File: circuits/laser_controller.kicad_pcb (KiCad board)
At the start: 4 copper layers, 173 x 61.1 mm, 180 parts, among them J1 USB_MINI_B, J2 USB_MINI_B, J5 24V DC IN, J6 CONN_RJ45, Q1 SOT-23, Q2 SOT-23, Q3 SOT-23, Q4 SOT-23, Q5 SOT-23, Q6 SOT-23, SW1 SW_PUSH, SW2 SW_PUSH, SW3 SW_PUSH, U1 SOIC-8_3.9x4.9mm_P1.27mm, U10 QFN-28-1EP_5x5mm_P0.5mm_EP3.3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, U11 SOT-23-5, U12 TSSOP-14_4.4x5mm_P0.65mm, U13 SOT-23, U14 LQFP-64_10x10mm_P0.5mm, U15 TSOT-23-6, U16 TSOT-23-6, U2 SOIC-8_3.9x4.9mm_P1.27mm, U3 SOIC-8_3.9x4.9mm_P1.27mm, U4 SOIC-8_3.9x4.9mm_P1.27mm, U5 SOT-23-5, U6 SOT-23-5, U7 SOT-23-5, U8 SOT-23-5, U9 ESP32-S3-WROOM-1

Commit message: fix(pcb): pull D8/C42 back from the board edge
D8 and C42 landed with negative edge clearance (-0.708mm / -0.055mm)
after the courtyard-overlap fix -- close enough to J1's cluster that
the solver satisfied the no-overlap constraint by pushing them partly
off the board outline instead. Re-solved both with an explicit board-
edge margin this time; still zero courtyard/pad overlaps.

Caught this because routing generated against the previous positions
produced segments with endpoints outside the board outline near D8 --
a good reminder to check edge clearance, not just inter-component
clearance, whenever placement changes.
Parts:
- moved D8 8.60 mm to (32.3, 81.3)
- moved C42 6.50 mm to (50.4, 83.9)
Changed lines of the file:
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@@
   )
   (footprint "D_SOD-523" (layer "F.Cu")
-    (at 40.893 80.417 90)
+    (at 32.340 81.316 90)
     (descr "http://www.diodes.com/datasheets/ap02001.pdf p.144")
     (tags "Diode SOD523")
@@
   )
   (footprint "C_0805_2012Metric_Pad1.18x1.45mm_HandSolder" (layer "F.Cu")
-    (at 44.675 80.800)
+    (at 50.402 83.875)
     (descr "Capacitor SMD 0805 (2012 Metric), square (rectangular) end terminal, IPC_7351 nominal with elongated pad for handsoldering. (Body size source: IPC-SM-782 page 76, https://www.pcb-3d.com/wordpress/wp-content/uploads/ipc-sm-782a_amendment_1_and_2.pdf, https://docs.google.com/spreadsheets/d/1BsfQQcO9C6DZCsRaXUlFlo91Tg2WpOkGARC1WS5S8t0/edit?usp=sharing), generated with kicad-footprint-generator")
     (tags "capacitor handsolder")

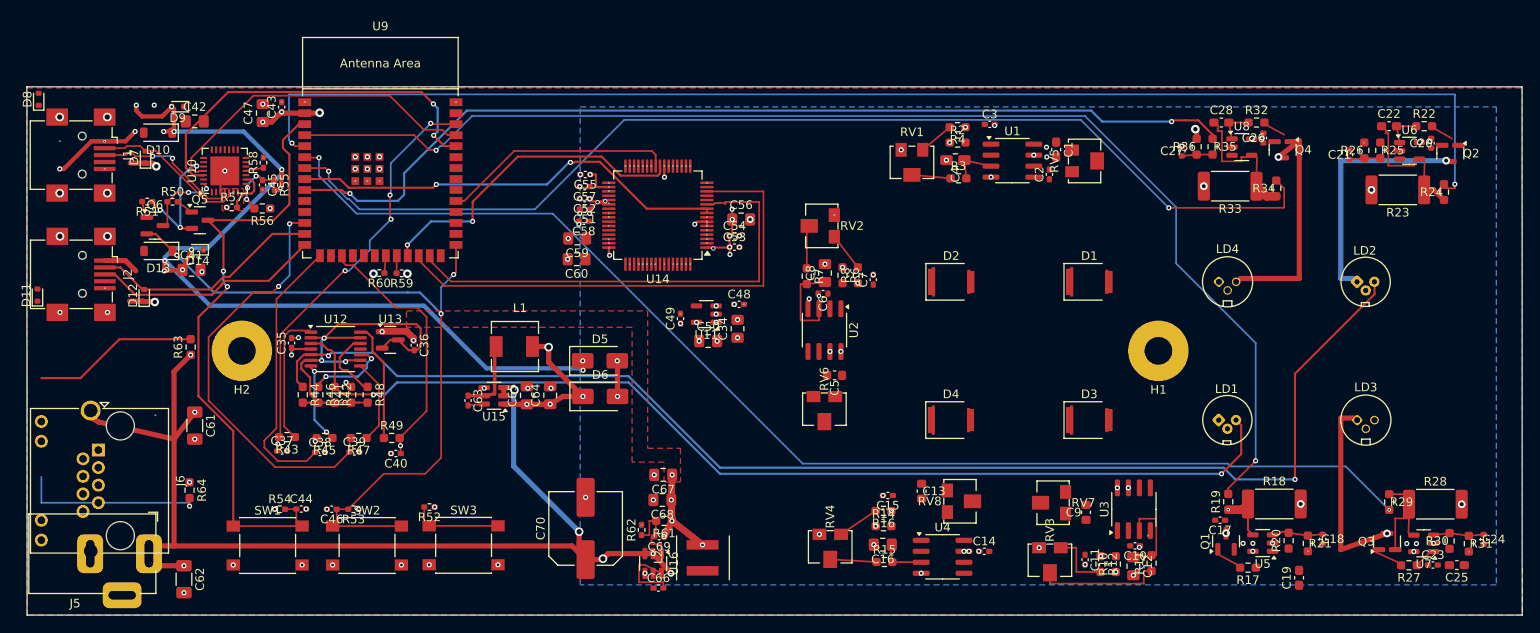
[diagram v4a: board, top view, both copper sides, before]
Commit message: fix(pcb): regenerate routing with clean power planes and full connectivity closure
Full re-route of laser_controller.kicad_pcb using the fixed router
engine (no via-on-pad, 45-degree chamfering, board-relative corridors)
against the now-overlap-free hand placement, plus a generic
connectivity-closure pass for nets no CRITICAL_ROUTE_LINKS/POWER_ROUTE_LINKS
entry covered at all (ADC bus signals, photodiode bias networks, AD7606
reference network).

Verified (all via check_laser_controller_pcb.py's own functions, not
self-reported):
- 0 footprint courtyard/pad overlaps (was 25)
- 0 different-net pad overlaps (was 4)
- 0 dangling copper
- 0 copper routed outside the board outline (was 13 -- two forced-route
  functions had stale absolute corridor coordinates from the board's
  original 90x50mm layout that placed copper entirely off the current
  173x61mm board; the router accepted them because clearance checks
  don't check board bounds, only other copper. Removed both.)
- 5 via-on-pad instances remain, all on intentionally-unnetted/NC pads
  (was ~176, nearly all on real signal pads)
- 70/110 multi-pad signal nets fully connected + 7 covered by a
  required zone/rail pour (was 10/111 critical links connected
  pre-regeneration)
- Zones: 9 clean, mutually non-overlapping definitions (was 9
  definitions with several overlapping bounding boxes on the same
  layer for different rails)

Remaining gap: ~33 multi-pad nets are still split, mostly long single-hop
MCU<->analog-cluster runs (PWM1-4, VOUT1-4, ISENSE1-4, MPD_RAWx, AD7606
SPI bus) that need corridor guidance this project's lightweight
grid-search router can't reliably find across 100+mm and ~170 other
footprints. Some locally-congested nets also picked up a via/layer
their strict net-class policy doesn't allow. Both are documented as
open items in PCB_LAYOUT.md/POWER_TREE.md; closing them is real manual
KiCad routing work, same as GUI ERC/DRC/visual return-path review were
already documented as pre-fabrication requ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
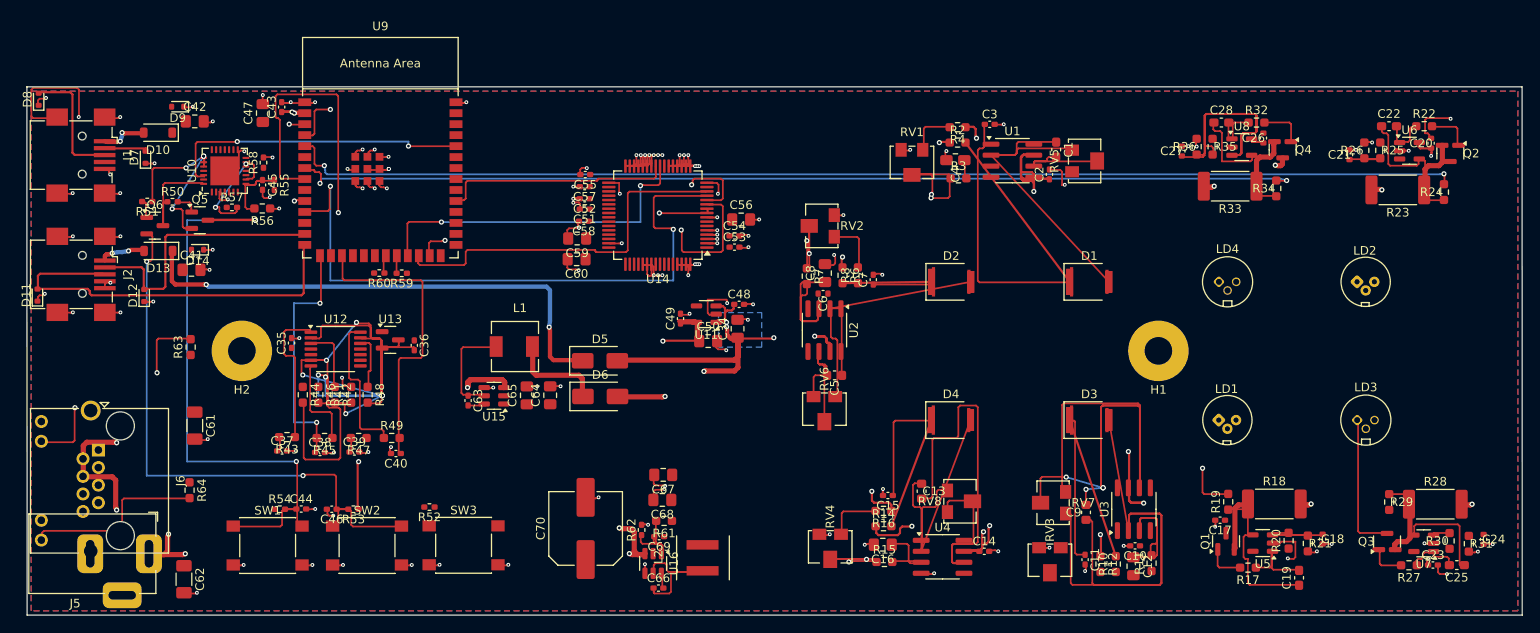
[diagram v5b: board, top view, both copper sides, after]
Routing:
- net +5V: track 17.1 -> 376.3 mm, vias 43 -> 19
- net GND: track 11.6 -> 227.5 mm, vias 156 -> 136
- net MPD_RAW2: track 152.0 -> 0.00 mm, vias 2 -> 0
- net ISENSE3: track 143.6 -> 0.00 mm, vias 2 -> 0
- net VIN_24V: track 131.1 -> 252.1 mm, vias 8 -> 7
- net MPD_RAW1: track 122.4 -> 7.67 mm, vias 2 -> 0
- net PWM4: track 113.2 -> 0.00 mm, vias 2 -> 0
- net /POWER_IO/MPD_BIAS: track 48.4 -> 138.9 mm, vias 3 -> 10
- net VOUT3: track 0.00 -> 90.3 mm, vias 0 -> 4
- net Net-(D3-A): track 0.00 -> 75.4 mm
- net ADC_CS: track 0.00 -> 74.1 mm, vias 0 -> 2
- net ADC_SCLK: track 0.00 -> 59.6 mm, vias 0 -> 2
- net +3V3: track 16.6 -> 73.1 mm, vias 23 -> 4
- net Net-(U8-+): track 3.56 -> 57.7 mm
- net VOUT4: track 0.00 -> 53.9 mm
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- added copper zone on B.Cu, net GND
- added copper zone on In2.Cu, net VIN_24V
- removed copper zone on F.Cu, net +3V3
- removed copper zone on F.Cu, net LASER_V+

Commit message: fix(pcb): close more long cross-board nets (larger route-search budget)
Follow-up connectivity pass with a 6x larger A* search budget (15000 vs
2500 cells) and a general-search fallback when no predefined corridor
lane is clear end-to-end. Closed several more PWM/ADC-bus links
(PWM1, PWM2, ADC_CS/SCLK/RESET/MISO_A, ISENSE1/2/4).

72/110 multi-pad nets now fully connected + 7 zone/rail-covered (was
70+7); via-on-pad down to 1 instance, and that one is J2 pin 4, an
intentionally-unconnected USB ID pin
(check_laser_controller_pcb.intentional_unnetted_pad_names already
allowlists it). 0 dangling copper, 0 pad overlaps, 0 copper outside
the board outline, unchanged from the previous commit.

Remaining 31 split nets (VOUT1-4, PWM3/4, MPD_RAWx, the AD7606
reference network, and a handful of local nodes in dense IC clusters)
are the stopping point for this project's lightweight router --
closing them is real manual KiCad routing work.
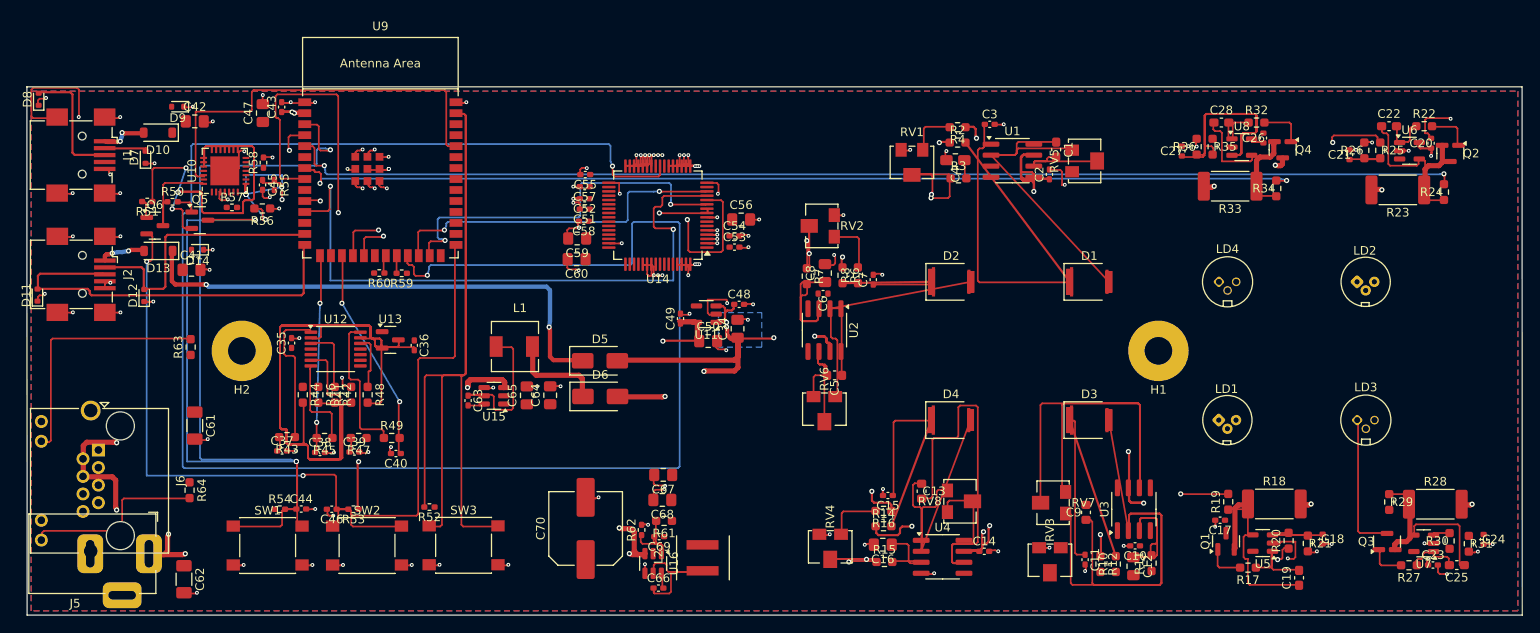
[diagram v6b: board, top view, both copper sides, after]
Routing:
- net PWM2: track 0.00 -> 232.9 mm, vias 0 -> 2
- net ADC_MISO_A: track 39.4 -> 221.6 mm
- net /MCU_ESP32-S3/FACT: track 0.00 -> 156.9 mm
- net PWM1: track 0.00 -> 152.5 mm, vias 0 -> 2
- net /POWER_IO/MPD_BIAS: track 138.9 -> 245.8 mm, vias 10 -> 0
- net /MCU_ESP32-S3/EN: track 91.6 -> 145.6 mm
- net /MCU_ESP32-S3/RTS: track 23.9 -> 69.9 mm
- net /MCU_ESP32-S3/PROG: track 68.0 -> 113.2 mm
- net VOUT3: track 90.3 -> 61.7 mm, vias 4 -> 0
- net ADC_MISO_B: track 26.7 -> 0.00 mm
- net Net-(U10-VBUS): track 10.2 -> 29.4 mm, vias 0 -> 6
- net Net-(U10-~{RST}): track 13.1 -> 0.00 mm, vias 2 -> 0
- net ADC_RESET: track 55.6 -> 43.9 mm
- net /MCU_ESP32-S3/IO44: track 35.6 -> 47.2 mm, vias 2 -> 0
- net MPD4: track 34.7 -> 25.0 mm, vias 0 -> 2
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
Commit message: fix(pcb): strip all routing, rebuild power zones to match access-controller
The previous auto-generated routing was rejected on review as low
quality (thick/tangled traces, crude bends) even though it had decent
net connectivity -- stripped entirely (0 segments, 0 vias) for a
from-scratch re-route.

Also fully reworked the power zones after the previous session's
small-isolated-pours approach was also rejected as overcomplicated.
Now matches ~/projects/access-controller/circuits/controller/
access-controller.kicad_pcb's pattern: a single full-board GND flood
on In1.Cu (no outer-layer GND fill -- F.Cu/B.Cu are pure signal
layers now), and In2.Cu split into exactly two simple, non-overlapping
rectangular regions (+3V3 over the MCU cluster, +5V over the
TIA/laser-driver clusters), with the POWER_IO buck/ADC/monitor
cluster left in the gap between them since it has real +3V3 and +5V
pins a few mm apart (U11/U12/U14) that neither region can honestly
claim.

Updated check_laser_controller_pcb.REQUIRED_PLANE_ZONES to drop the
now-removed B.Cu +5V requirement.

Found and fixed a real gap along the way: writing a zone's polygon
outline with `fill yes` set is not the same as it having real copper
-- KiCad only writes the computed `filled_polygon` data (what
gerbers/renders are generated from) when its own zone-fill algorithm
actually runs, and the project's own required_plane_zone_failures
check only looks for the `fill yes` text flag, not filled_polygon
presence. Every zone this project has generated all session had
outline-only shells with no computed fill. Filled properly via the
pcbnew Python API (pcbnew.ZONE_FILLER(board).Fill(board.Zones())) and
verified visually via kicad-cli SVG export -- both the GND plane and
the two power regions now render as real filled copper. Also
confirmed the round-trip through pcbnew preserves everything the
project's own regex-based parsers depend on.

Verified via check_laser_controller_pcb.py's own functions: 0
footprint courtyard overlap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
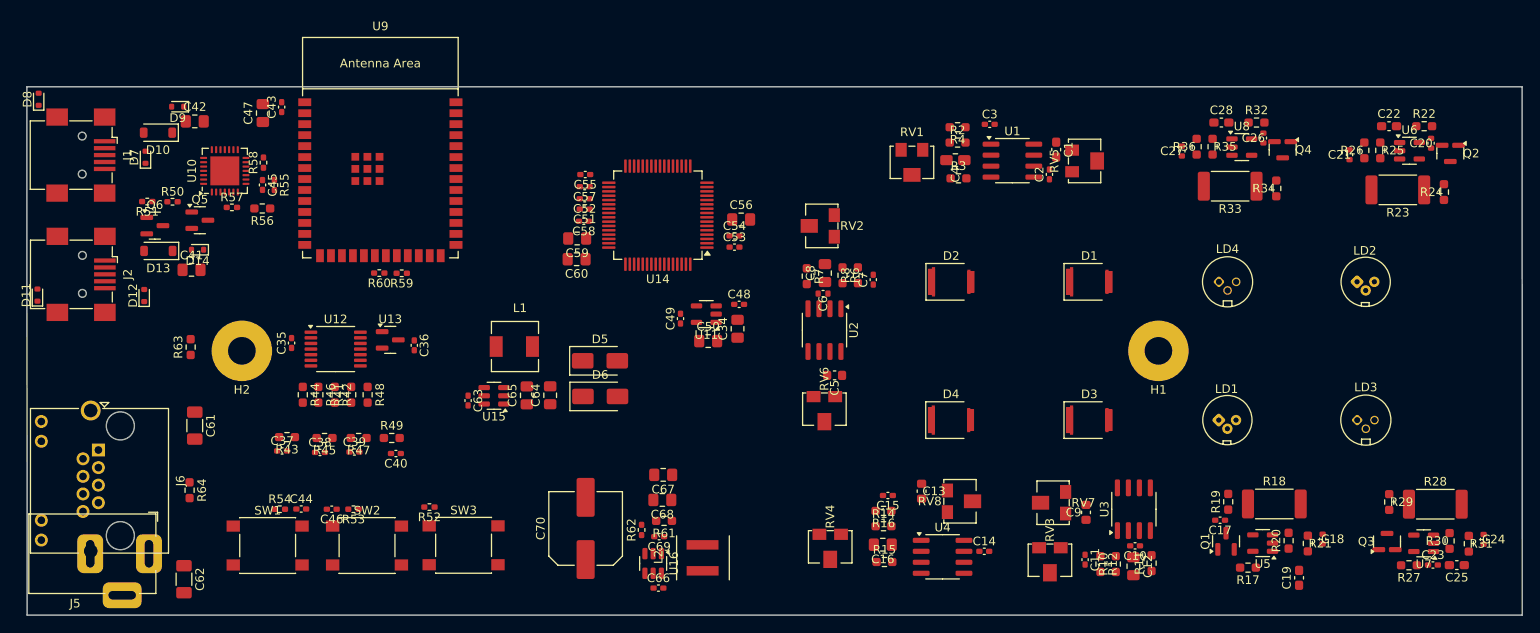
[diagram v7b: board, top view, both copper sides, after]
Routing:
- net +5V: track 376.3 -> 0.00 mm, vias 19 -> 0
- net VIN_24V: track 252.1 -> 0.00 mm, vias 7 -> 0
- net /POWER_IO/MPD_BIAS: track 245.8 -> 0.00 mm
- net PWM2: track 232.9 -> 0.00 mm, vias 2 -> 0
- net GND: track 227.5 -> 0.00 mm, vias 136 -> 0
- net ADC_MISO_A: track 221.6 -> 0.00 mm, vias 2 -> 0
- net /MCU_ESP32-S3/FACT: track 156.9 -> 0.00 mm
- net PWM1: track 152.5 -> 0.00 mm, vias 2 -> 0
- net ISENSE1: track 151.2 -> 0.00 mm, vias 2 -> 0
- net /MCU_ESP32-S3/EN: track 145.6 -> 0.00 mm, vias 4 -> 0
- net ISENSE2: track 135.8 -> 0.00 mm, vias 2 -> 0
- net ISENSE4: track 117.1 -> 0.00 mm, vias 2 -> 0
- net /MCU_ESP32-S3/PROG: track 113.2 -> 0.00 mm, vias 2 -> 0
- net CONVST: track 76.7 -> 0.00 mm, vias 2 -> 0
- net Net-(D3-A): track 75.4 -> 0.00 mm
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- removed copper zone on B.Cu, net +5V
- removed copper zone on B.Cu, net GND
- removed copper zone on F.Cu, net GND
- removed copper zone on In2.Cu, net LASER_V+
- removed copper zone on In2.Cu, net VIN_24V

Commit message: wip(pcb): manual routing in progress (KiCad GUI)
Real hand-routing progress since the routing strip: 1130 segments,
188 vias added. Verified before committing: file parses cleanly (180
footprints, no dup refs), 0 different-net pad overlaps, 0 copper
outside the board outline, 1 dangling segment (likely mid-edit).

Connectivity: 85/110 multi-pad nets fully connected + 4 covered by a
required zone/rail pour, 21 still split -- ahead of where the
automated routing attempts landed (72/110 + 7).
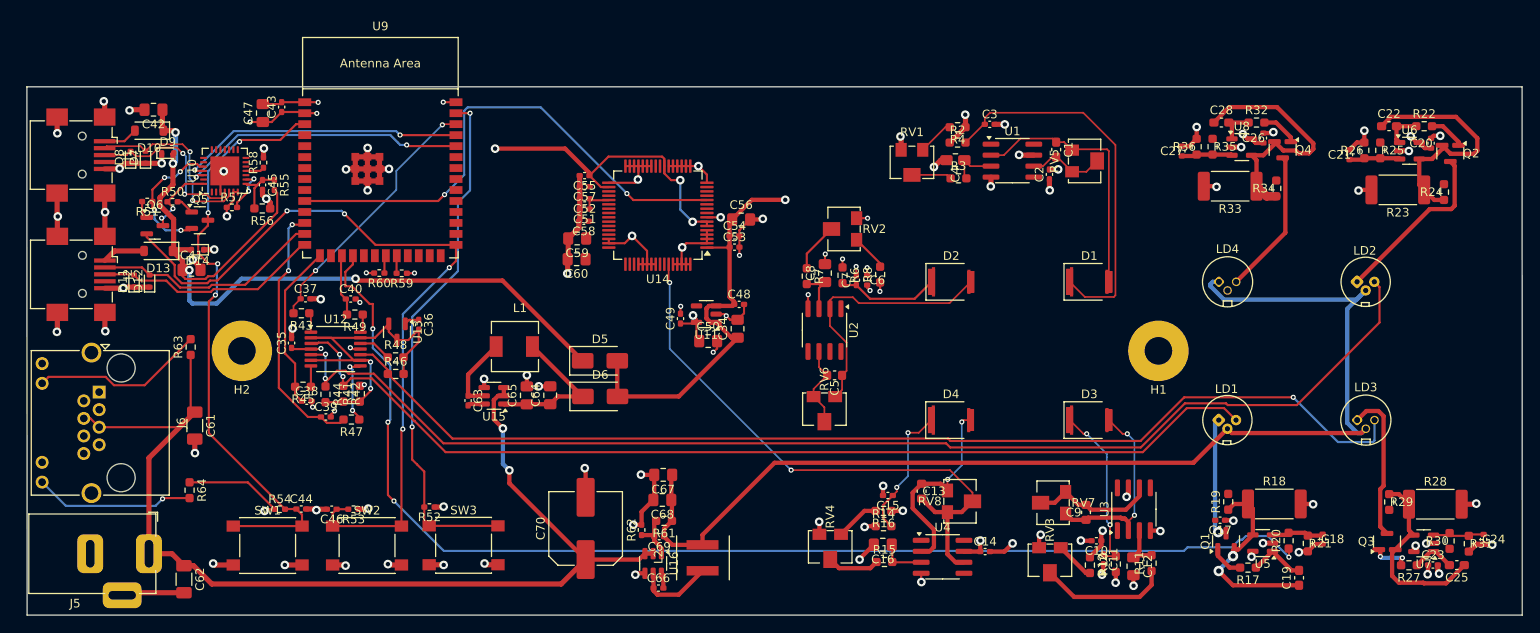
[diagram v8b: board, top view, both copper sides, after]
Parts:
- moved C40 18.6 mm to (68.4, 104.4), turned to 0 degrees
- moved C37 17.8 mm to (63.2, 104.4)
- moved R49 14.9 mm to (68.9, 106.2), turned to 180 degrees
- moved R43 14.4 mm to (62.7, 106.1)
- moved D8 12.6 mm to (43.0, 88.0)
- moved D11 11.3 mm to (43.4, 102.3)
- moved R46 9.27 mm to (73.7, 113.1), turned to 0 degrees
- moved J6 6.71 mm to (39.3, 115.2)
- moved R45 6.43 mm to (62.9, 114.6)
- moved C38 6.13 mm to (63.4, 116.2)
- moved D9 5.50 mm to (47.3, 87.5), turned to 0 degrees
- moved R48 5.41 mm to (73.6, 111.2), turned to 0 degrees
- moved C6 5.33 mm to (128.2, 102.2), turned to -90 degrees
- moved C39 5.23 mm to (65.6, 118.1)
- moved C42 4.96 mm to (45.6, 82.5), turned to 180 degrees
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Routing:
- net GND: track 0.00 -> 230.9 mm, vias 0 -> 89
- net MPD_RAW2: track 0.00 -> 143.3 mm, vias 0 -> 2
- net PWM1: track 0.00 -> 140.6 mm, vias 0 -> 4
- net LASER_V+: track 0.00 -> 137.0 mm
- net MPD_RAW3: track 0.00 -> 128.4 mm, vias 0 -> 1
- net VIN_24V: track 0.00 -> 125.8 mm, vias 0 -> 2
- net MPD_RAW1: track 0.00 -> 117.6 mm, vias 0 -> 2
- net VBUS_5V: track 0.00 -> 98.1 mm, vias 0 -> 4
- net /MCU_ESP32-S3/PROG: track 0.00 -> 90.8 mm, vias 0 -> 4
- net +5V: track 0.00 -> 84.4 mm, vias 0 -> 19
- net +3V3: track 0.00 -> 73.3 mm, vias 0 -> 13
- net /MCU_ESP32-S3/EN: track 0.00 -> 70.2 mm, vias 0 -> 4
- net VOUT4: track 0.00 -> 67.0 mm, vias 0 -> 2
- net /MCU_ESP32-S3/FACT: track 0.00 -> 60.9 mm, vias 0 -> 2
- net ADC_SCLK: track 0.00 -> 59.8 mm, vias 0 -> 2
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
